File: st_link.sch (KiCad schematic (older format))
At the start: 26 parts, among them J2 Conn_01x05, Q1 AO3402, U1 AMS1117-3.3, U2 STM32F103C8Tx, Y1 Crystal_GND24

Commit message: sch: List LCSC P/N for each component
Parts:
- C1, C10, C11, C2, C3, C4, C9: LCSC P/N (none) -> C1591; MFR P/N (none) -> CL10B104KB8NNNC
- C5, C8: LCSC P/N (none) -> C19702; MFR P/N (none) -> CL10A106KP8NNNC
- C6, C7: LCSC P/N (none) -> C95843; MFR P/N (none) -> CL10B105KP8NNNC
- D1: LCSC P/N (none) -> C157741; MFR P/N (none) -> LTST-C193KRKT-5A
- D2: LCSC P/N (none) -> C125102; MFR P/N (none) -> LTST-C193KGKT-5A
- J2: LCSC P/N (none) -> C138801; MFR P/N (none) -> C138801
- Q1: LCSC P/N (none) -> C427384; MFR P/N (none) -> AO3402
- R1, R6, R7: LCSC P/N (none) -> C115324; MFR P/N (none) -> RS-03K1002FT
- R10: LCSC P/N (none) -> C115420; MFR P/N (none) -> RS-03K1000FT
- R2: LCSC P/N (none) -> C327826; MFR P/N (none) -> MR06X1003FTL
- R5: LCSC P/N (none) -> C118397; MFR P/N (none) -> RS-03K1501FT
- R8, R9: LCSC P/N (none) -> C380759; MFR P/N (none) -> SY0603JN1KP
- U1: LCSC P/N (none) -> C426566; MFR P/N (none) -> AMS1117-3.3
- U2: LCSC P/N (none) -> C8734; MFR P/N (none) -> STM32F103C8T6
- Y1: LCSC P/N (none) -> C400090; MFR P/N (none) -> TAXM8M4RDBCCT2T
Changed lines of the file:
@@
 F 2 "Package_QFP:LQFP-48_7x7mm_P0.5mm" H 3100 3100 50  0001 R CNN
 F 3 "http://www.st.com/st-web-ui/static/active/en/resource/technical/document/datasheet/CD00161566.pdf" H 3700 4500 50  0001 C CNN
+F 4 "C8734" H 3700 4500 50  0001 C CNN "LCSC P/N"
+F 5 "STM32F103C8T6" H 3700 4500 50  0001 C CNN "MFR P/N"
 	1    3700 4500
 	1    0    0    -1
@@
 F 2 "Resistor_SMD:R_0603_1608Metric" H 2700 3400 50  0001 C CNN
 F 3 "~" H 2700 3400 50  0001 C CNN
+F 4 "C115324" H 2700 3400 50  0001 C CNN "LCSC P/N"
+F 5 "RS-03K1002FT" H 2700 3400 50  0001 C CNN "MFR P/N"
 	1    2700 3400
 	0    -1   1    0
@@
 F 2 "Resistor_SMD:R_0603_1608Metric" H 2400 3000 50  0001 C CNN
 F 3 "~" H 2400 3000 50  0001 C CNN
+F 4 "C327826" H 2400 3000 50  0001 C CNN "LCSC P/N"
+F 5 "MR06X1003FTL" H 2400 3000 50  0001 C CNN "MFR P/N"
 	1    2400 3000
 	1    0    0    -1
@@
 F 2 "Capacitor_SMD:C_0603_1608Metric" H 2200 3200 50  0001 C CNN
 F 3 "~" H 2200 3200 50  0001 C CNN
+F 4 "C1591" H 2200 3200 50  0001 C CNN "LCSC P/N"
+F 5 "CL10B104KB8NNNC" H 2200 3200 50  0001 C CNN "MFR P/N"
 	1    2200 3200
 	0    -1   1    0
@@
 F 2 "Resistor_SMD:R_0603_1608Metric" H 2700 3900 50  0001 C CNN
 F 3 "~" H 2700 3900 50  0001 C CNN
+F 4 "C115324" H 2700 3900 50  0001 C CNN "LCSC P/N"
+F 5 "RS-03K1002FT" H 2700 3900 50  0001 C CNN "MFR P/N"
 	1    2700 3900
 	0    -1   1    0
@@
 F 2 "Capacitor_SMD:C_0603_1608Metric" H 1550 4100 50  0001 C CNN
 F 3 "~" H 1550 4100 50  0001 C CNN
+F 4 "C1591" H 1550 4100 50  0001 C CNN "LCSC P/N"
+F 5 "CL10B104KB8NNNC" H 1550 4100 50  0001 C CNN "MFR P/N"
 	1    1550 4100
 	-1   0    0    -1
@@
 F 2 "Capacitor_SMD:C_0603_1608Metric" H 2050 4100 50  0001 C CNN
 F 3 "~" H 2050 4100 50  0001 C CNN
+F 4 "C1591" H 2050 4100 50  0001 C CNN "LCSC P/N"
+F 5 "CL10B104KB8NNNC" H 2050 4100 50  0001 C CNN "MFR P/N"
 	1    2050 4100
 	-1   0    0    -1
@@
 F 2 "Resistor_SMD:R_0603_1608Metric" H 2700 5500 50  0001 C CNN
 F 3 "~" H 2700 5500 50  0001 C CNN
+F 4 "C115420" H 2700 5500 50  0001 C CNN "LCSC P/N"
+F 5 "RS-03K1000FT" H 2700 5500 50  0001 C CNN "MFR P/N"
 	1    2700 5500
 	0    -1   1    0
@@
 F 2 "Resistor_SMD:R_0603_1608Metric" H 5050 5350 50  0001 C CNN
 F 3 "~" H 5050 5350 50  0001 C CNN
+F 4 "C380759" H 5050 5350 50  0001 C CNN "LCSC P/N"
+F 5 "SY0603JN1KP" H 5050 5350 50  0001 C CNN "MFR P/N"
 	1    5050 5350
 	-1   0    0    -1
@@
 F 2 "LED_SMD:LED_0603_1608Metric" V 5050 5600 50  0001 C CNN
 F 3 "~" V 5050 5600 50  0001 C CNN
+F 4 "C125102" H 5050 5600 50  0001 C CNN "LCSC P/N"
+F 5 "LTST-C193KGKT-5A" H 5050 5600 50  0001 C CNN "MFR P/N"
 	1    5050 5600
 	0    -1   -1   0
@@
 F 2 "Resistor_SMD:R_0603_1608Metric" H 5050 5050 50  0001 C CNN
 F 3 "~" H 5050 5050 50  0001 C CNN
+F 4 "C380759" H 5050 5050 50  0001 C CNN "LCSC P/N"
+F 5 "SY0603JN1KP" H 5050 5050 50  0001 C CNN "MFR P/N"
 	1    5050 5050
 	-1   0    0    -1
@@
 F 2 "LED_SMD:LED_0603_1608Metric" V 5050 4800 50  0001 C CNN
 F 3 "~" V 5050 4800 50  0001 C CNN
+F 4 "C157741" H 5050 4800 50  0001 C CNN "LCSC P/N"
+F 5 "LTST-C193KRKT-5A" H 5050 4800 50  0001 C CNN "MFR P/N"
 	1    5050 4800
 	0    -1   -1   0
@@
 F 2 "Package_TO_SOT_SMD:SOT-23" H 8050 3875 50  0001 L CIN
 F 3 "http://www.aosmd.com/pdfs/datasheet/AO3402.pdf" H 7850 3950 50  0001 L CNN
+F 4 "C427384" H 7850 3950 50  0001 C CNN "LCSC P/N"
+F 5 "AO3402" H 7850 3950 50  0001 C CNN "MFR P/N"
 	1    7850 3950
 	1    0    0    -1
@@
 F 2 "Resistor_SMD:R_0603_1608Metric" H 7950 4350 50  0001 C CNN
 F 3 "~" H 7950 4350 50  0001 C CNN
+F 4 "C118397" H 7950 4350 50  0001 C CNN "LCSC P/N"
+F 5 "RS-03K1501FT" H 7950 4350 50  0001 C CNN "MFR P/N"
 	1    7950 4350
 	-1   0    0    -1
@@
 F 2 "Resistor_SMD:R_0603_1608Metric" H 7750 3650 50  0001 C CNN
 F 3 "~" H 7750 3650 50  0001 C CNN
+F 4 "C115324" H 7750 3650 50  0001 C CNN "LCSC P/N"
+F 5 "RS-03K1002FT" H 7750 3650 50  0001 C CNN "MFR P/N"
 	1    7750 3650
 	0    1    -1   0
@@
 F 2 "Capacitor_SMD:C_0603_1608Metric" H 8750 1650 50  0001 C CNN
 F 3 "~" H 8750 1650 50  0001 C CNN
+F 4 "C1591" H 8750 1650 50  0001 C CNN "LCSC P/N"
+F 5 "CL10B104KB8NNNC" H 8750 1650 50  0001 C CNN "MFR P/N"
 	1    8750 1650
 	-1   0    0    -1
@@
 F 2 "Capacitor_SMD:C_0603_1608Metric" H 9150 1650 50  0001 C CNN
 F 3 "~" H 9150 1650 50  0001 C CNN
+F 4 "C1591" H 9150 1650 50  0001 C CNN "LCSC P/N"
+F 5 "CL10B104KB8NNNC" H 9150 1650 50  0001 C CNN "MFR P/N"
 	1    9150 1650
 	-1   0    0    -1
@@
 F 2 "Capacitor_SMD:C_0603_1608Metric" H 9550 1650 50  0001 C CNN
 F 3 "~" H 9550 1650 50  0001 C CNN
+F 4 "C1591" H 9550 1650 50  0001 C CNN "LCSC P/N"
+F 5 "CL10B104KB8NNNC" H 9550 1650 50  0001 C CNN "MFR P/N"
 	1    9550 1650
 	-1   0    0    -1
@@
 F 2 "Capacitor_SMD:C_0603_1608Metric" H 9950 1650 50  0001 C CNN
 F 3 "~" H 9950 1650 50  0001 C CNN
+F 4 "C1591" H 9950 1650 50  0001 C CNN "LCSC P/N"
+F 5 "CL10B104KB8NNNC" H 9950 1650 50  0001 C CNN "MFR P/N"
 	1    9950 1650
 	-1   0    0    -1
@@
 F 2 "Connector_PinHeader_2.54mm:PinHeader_1x05_P2.54mm_Vertical" H 9950 5400 50  0001 C CNN
 F 3 "~" H 9950 5400 50  0001 C CNN
+F 4 "C138801" H 9950 5400 50  0001 C CNN "LCSC P/N"
+F 5 "C138801" H 9950 5400 50  0001 C CNN "MFR P/N"
 	1    9950 5400
 	1    0    0    -1
@@
 F 2 "Package_TO_SOT_SMD:SOT-223-3_TabPin2" H 6250 2400 50  0001 C CNN
 F 3 "http://www.advanced-monolithic.com/pdf/ds1117.pdf" H 6350 1950 50  0001 C CNN
+F 4 "C426566" H 6250 2200 50  0001 C CNN "LCSC P/N"
+F 5 "AMS1117-3.3" H 6250 2200 50  0001 C CNN "MFR P/N"
 	1    6250 2200
 	1    0    0    -1
@@
 F 2 "Capacitor_SMD:C_0603_1608Metric" H 6650 2400 50  0001 C CNN
 F 3 "~" H 6650 2400 50  0001 C CNN
+F 4 "C95843" H 6650 2400 50  0001 C CNN "LCSC P/N"
+F 5 "CL10B105KP8NNNC" H 6650 2400 50  0001 C CNN "MFR P/N"
 	1    6650 2400
 	-1   0    0    -1
@@
 F 2 "Capacitor_SMD:C_0603_1608Metric" H 7050 2400 50  0001 C CNN
 F 3 "~" H 7050 2400 50  0001 C CNN
+F 4 "C19702" H 7050 2400 50  0001 C CNN "LCSC P/N"
+F 5 "CL10A106KP8NNNC" H 7050 2400 50  0001 C CNN "MFR P/N"
 	1    7050 2400
 	-1   0    0    -1
@@
 F 2 "Capacitor_SMD:C_0603_1608Metric" H 5450 2400 50  0001 C CNN
 F 3 "~" H 5450 2400 50  0001 C CNN
+F 4 "C19702" H 5450 2400 50  0001 C CNN "LCSC P/N"
+F 5 "CL10A106KP8NNNC" H 5450 2400 50  0001 C CNN "MFR P/N"
 	1    5450 2400
 	1    0    0    1
@@
 F 2 "Capacitor_SMD:C_0603_1608Metric" H 5850 2400 50  0001 C CNN
 F 3 "~" H 5850 2400 50  0001 C CNN
+F 4 "C95843" H 5850 2400 50  0001 C CNN "LCSC P/N"
+F 5 "CL10B105KP8NNNC" H 5850 2400 50  0001 C CNN "MFR P/N"
 	1    5850 2400
 	1    0    0    1
@@
 F 2 "Crystal:Crystal_SMD_3225-4Pin_3.2x2.5mm" H 1800 3900 50  0001 C CNN
 F 3 "~" H 1800 3900 50  0001 C CNN
+F 4 "C400090" H 1800 3900 50  0001 C CNN "LCSC P/N"
+F 5 "TAXM8M4RDBCCT2T" H 1800 3900 50  0001 C CNN "MFR P/N"
 	1    1800 3900
 	1    0    0    -1

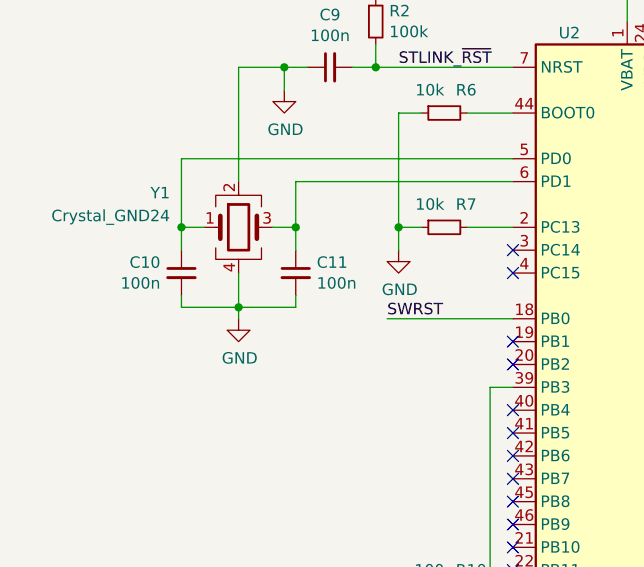
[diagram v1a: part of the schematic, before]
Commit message: sch: Fix quartz load capacitors values
They were 100n, thanks copy/paste..
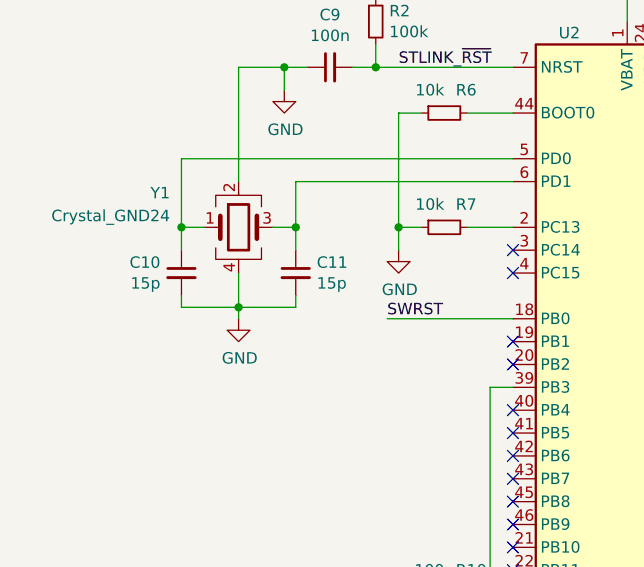
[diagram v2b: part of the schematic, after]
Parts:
- C10, C11: value 100n -> 15p; LCSC P/N C1591 -> C1644; MFR P/N CL10B104KB8NNNC -> CL10C150JB8NNNC
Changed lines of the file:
@@
 P 1550 4100
 F 0 "C10" H 1642 4146 50  0000 L CNN
-F 1 "100n" H 1642 4055 50  0000 L CNN
+F 1 "15p" H 1642 4055 50  0000 L CNN
 F 2 "Capacitor_SMD:C_0603_1608Metric" H 1550 4100 50  0001 C CNN
 F 3 "~" H 1550 4100 50  0001 C CNN
-F 4 "C1591" H 1550 4100 50  0001 C CNN "LCSC P/N"
-F 5 "CL10B104KB8NNNC" H 1550 4100 50  0001 C CNN "MFR P/N"
+F 4 "C1644" H 1550 4100 50  0001 C CNN "LCSC P/N"
+F 5 "CL10C150JB8NNNC" H 1550 4100 50  0001 C CNN "MFR P/N"
 	1    1550 4100
 	-1   0    0    -1
@@
 P 2050 4100
 F 0 "C11" H 1958 4146 50  0000 R CNN
-F 1 "100n" H 1958 4055 50  0000 R CNN
+F 1 "15p" H 1958 4055 50  0000 R CNN
 F 2 "Capacitor_SMD:C_0603_1608Metric" H 2050 4100 50  0001 C CNN
 F 3 "~" H 2050 4100 50  0001 C CNN
-F 4 "C1591" H 2050 4100 50  0001 C CNN "LCSC P/N"
-F 5 "CL10B104KB8NNNC" H 2050 4100 50  0001 C CNN "MFR P/N"
+F 4 "C1644" H 2050 4100 50  0001 C CNN "LCSC P/N"
+F 5 "CL10C150JB8NNNC" H 2050 4100 50  0001 C CNN "MFR P/N"
 	1    2050 4100
 	-1   0    0    -1
